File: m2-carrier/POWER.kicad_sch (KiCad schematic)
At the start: 0 parts

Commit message: new stuff
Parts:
- added C16: 4700pF, symbol Device:C_Small
- added C17: 47pF, symbol Device:C_Small
- added C18: 0.1uF, symbol Device:C_Small
- added C19, C20, C21: 47uF, symbol Device:C_Small
- added C21 (x5), C23: 2.2uF, Capacitor_SMD:C_0402_1005Metric, symbol Device:C_Small
- added C24, C27: 47uF, Capacitor_SMD:C_0402_1005Metric, symbol Device:C_Small
- added C28, C29, C32: 100nF, Capacitor_SMD:C_0402_1005Metric, symbol Device:C_Small
- added C3, C5: 10uF, Capacitor_SMD:C_0402_1005Metric_Pad0.74x0.62mm_HandSolder, symbol Device:C_Small
- added C30: 10uF, Capacitor_SMD:C_0402_1005Metric, symbol Device:C_Small
- added C31: C_SS, Capacitor_SMD:C_0402_1005Metric, symbol Device:C_Small
- added D3: D_Small, symbol Device:D_Small
- added D7: B340AG, Diode_SMD:D_SMB, symbol Device:D_Schottky_Small
- added D8: MMBZ5242B, Diode_SMD:D_SOT-23_ANK, symbol Diode:BZV55C12
- added JP1: SolderJumper_3_Open, Jumper:SolderJumper-3_P1.3mm_Open_RoundedPad1.0x1.5mm_NumberLabels, symbol Jumper:SolderJumper_3_Open
- added JP3: IO_EN, Jumper:SolderJumper-2_P1.3mm_Open_RoundedPad1.0x1.5mm, symbol Jumper:SolderJumper_2_Open
- added L2: 8.2uH, Inductor_SMD:L_Bourns_SRP7028A_7.3x6.6mm, symbol Device:L_Small
- added L2: L_Small, symbol Device:L_Small
- added P1: ESC1_VCC, TestPoint:TestPoint_Pad_2.0x2.0mm, symbol hermes_v1-rescue:PAD_SMD-pkl_misc
- added P2: ESC1_GND, TestPoint:TestPoint_Pad_D2.0mm, symbol hermes_v1-rescue:PAD_SMD-pkl_misc
- added P3: LIPO_VCC, TestPoint:TestPoint_Pad_2.0x2.0mm, symbol hermes_v1-rescue:PAD_SMD-pkl_misc
- added P4: LIPO_GND, TestPoint:TestPoint_Pad_D2.0mm, symbol hermes_v1-rescue:PAD_SMD-pkl_misc
- added P5: ESC2_VCC, TestPoint:TestPoint_Pad_2.0x2.0mm, symbol hermes_v1-rescue:PAD_SMD-pkl_misc
- added P6: ESC2_GND, TestPoint:TestPoint_Pad_D2.0mm, symbol hermes_v1-rescue:PAD_SMD-pkl_misc
- added Q1: DMP3013SFV, Package_SON:Diodes_PowerDI3333-8, symbol Transistor_FET:DMP3013SFV
- added R10: 53.6K, symbol Device:R_Small
- added R10: 49.9K, Resistor_SMD:R_0402_1005Metric, symbol Device:R_Small
- added R11: 17.8K, Resistor_SMD:R_0402_1005Metric, symbol Device:R_Small
- added R11: 10.2K, symbol Device:R_Small
- added R17: 12K, Resistor_SMD:R_0402_1005Metric, symbol Device:R_Small
- added R6: 442K, symbol Device:R_Small
- added R7: 90.9K, symbol Device:R_Small
- added R8: 100K, Resistor_SMD:R_0402_1005Metric, symbol Device:R_Small
- added R8: 243K, symbol Device:R_Small
- added R9: 16.9K, symbol Device:R_Small
- added U2: LD1117S33TR_SOT223, Package_TO_SOT_SMD:SOT-223-3_TabPin2, symbol Regulator_Linear:LD1117S33TR_SOT223
- added U3: TPS54560DDAR, Package_SO:Texas_R-PDSO-G8_EP2.95x4.9mm_Mask2.4x3.1mm, symbol Regulator_Switching:TPS54560BDDA
- added U6: LMR16030SDDAR, Package_SO:Texas_HSOP-8-1EP_3.9x4.9mm_P1.27mm_ThermalVias, symbol Regulator_Switching:LMR33630ADDA
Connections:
- new net: C31.1, U6.6 (VCC)
- new net: C29.2, D8.2 (A), Q1.4 (G), R17.1
- new net: C16.1, R9.2
- new net: C21.1, C21.1, C21.1, C21.1, R6.1, U3.2 (VIN)
- new net: R6.2, R7.1, U3.3 (EN)
- new net: C32.2, D7.1 (K), L2.1, U6.8 (SW)
- new net: C32.1, U6.1 (PGND)
- new net: R10.1, U6.4 (PG)
- new net: C18.2, U3.1 (BOOT)
- new net: R8.1, U3.4 (RT/CLK)
- new net: C18.1, D3.1 (K), L2.1, U3.8 (SW)
- new net +12v: C21.1, C23.1, U6.2 (VIN)
- new net +3V3: C5.1, JP3.1 (A), U2.2 (VO)
- new net +5V: JP1.3 (B)
- new net 15V: C29.1, C30.1, D8.1 (K), Q1.1 (S), Q1.2 (S), Q1.3 (S)
- new net 3V3_IO: JP3.2 (B)
- new net 5V_FC_VDD: C24.2, C27.2, L2.2, R8.1
- new net 5V_SERVO_VDD: C19.1, C20.1, C21.1, L2.2, R10.1
- new net COMP: C17.1, R9.1, U3.6 (COMP)
- new net FB: R10.2, R11.1, R11.1, R8.2, U3.5 (FB), U6.5 (FB)
- new net FC_USB_VBUS: JP1.1 (A)
- new net GND: C16.2, C17.2, C19.2, C20.2, C21.2, C21.2, C21.2, C21.2, C21.2, C21.2, C23.2, C24.1, C27.1, C28.2, C3.2, C30.2, C31.2, C5.2, D3.2 (A), D7.2 (A), P2.1 (PAD), P4.1 (PAD), P6.1 (PAD), R10.2, R11.2, R11.2, R17.2, R7.2, R8.2, U2.1 (GND), U3.7 (GND), U3.9 (GND), U6.7 (BOOT), U6.9 (AGND)
- new net REG_5VIN: C3.1, JP1.2 (C), U2.3 (VI)
- new net VCC: C28.1, P1.1 (PAD), P3.1 (PAD), P5.1 (PAD), Q1.5 (D)
- no-connect marks 0 -> 1
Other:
- note added: "+5V @ 3A DC-DC Converter Flight Controller 5V (4.3v-60v Input)"
- note added: "+5V @ 5A DC-DC Converter Servos 5V (7v-60v Input)"
- note added: "2.1mm Tip +12v input Voltage"
- note added: "3A RMS Current 6A I_Saturation"
- note added: "By default, the usb port are connected to the 3.3V LDO If bridged, LDO receives power from buck regulator"
- note added: "C_BOOT"
- note added: "C_SS"
- note added: "Diode to prevent reverse polarity at input"
- note added: "ESC Solder Pads"
- note added: "LiPo Battery Solder Pads"
- note added: "Linear Dropout Regulator - LD1117 - 3.3V 1A"
- note added: "Maximum input voltage: 26V"
- note added: "R_FBB"
- note added: "R_FBT"
- note added: "Rated for 16V"
- note added: "SOT23-3 225mW-300mW"
- note added: "Solder-Jumper for USB_VBUS and 5V"

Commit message: added video IC
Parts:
- added C22, C26: 10uF, Capacitor_SMD:C_0603_1608Metric, symbol Device:C_Small
- added C23, C24: 10uF, Capacitor_SMD:C_0805_2012Metric, symbol Device:C_Small
- added C25: 100nF, symbol Device:C_Small
- added C27, C28, C29: 22uF, Capacitor_SMD:C_0805_2012Metric, symbol Device:C_Small
- added JP1: USB1, Jumper:SolderJumper-3_P1.3mm_Open_RoundedPad1.0x1.5mm_NumberLabels, symbol Jumper:SolderJumper_3_Open
- added L3: 1.5uH, symbol Device:L_Small
- added R13: 10K, symbol Device:R_Small
- added R14: 402K, symbol Device:R_Small
- added R15: 39K, symbol Device:R_Small
- added R16: 100K, symbol Device:R_Small
- added U6: TPS63070RNMR, TPS63070RNMR:RNM0015A, symbol 2023-11-30_05-20-42:TPS63070RNMR
- D3: value D_Small -> B560C
- JP1: value SolderJumper_3_Open -> USB0
- L2: value L_Small -> 7.2uH
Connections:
- net +12v is gone; now on net 15V: C21.1, C23.1, U6.2 (VIN)
- net +5V is gone; now on net 5V_FC_VDD: JP1.3 (B)
- net 3V3_IO is gone; now on net 3V3_FC_VDD: JP3.2 (B)
- net 15V: now also C21.1, C21.1, C21.1, C21.1, R6.1, U3.2 (VIN), C22.1, C23.1, C24.1, R13.1, U6.12 (VIN), U6.13 (VIN)
- net 5V_FC_VDD: now also JP1.3 (B)
- net GND: now also C22.2, C23.2, C24.2, C25.2, C27.2, C28.2, C29.2, R15.2, U6.10 (PGND), U6.15 (VSEL), U6.4 (GND), U6.6 (FB2)
- net +3V3 renamed 3V3_FC_VDD
- net 3V3_FC_VDD: no longer JP3.1 (A)
- net FC_USB_VBUS renamed PWR_USB0_VBUS
- net REG_5VIN renamed 5V_VREG_IN
- net 5V_VREG_IN: now also JP1.2 (C)
- new net: R14.2, R15.1, U6.5 (FB)
- new net: R13.2, U6.1 (PS_SYNC), U6.14 (EN)
- new net: L3.1, U6.11 (L1)
- new net: R16.2, U6.2 (PG)
- new net: L3.2, U6.9 (L2)
- new net 3V3_IO_VDD: JP3.1 (A)
- new net 9V_CAMERA_VDD: C26.1, C27.1, C28.1, C29.1, R14.1, R16.1, U6.7 (VOUT), U6.8 (VOUT)
- new net PWR_USB1_VBUS: JP1.1 (A)
- new net VAUX: C25.1, U6.3 (VAUX)
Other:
- note added: "+9V @ 3.6A DC-DC Converter Camera & VTX 9V (7v-60v Input)"
- note added: "Solder-Jumper for 3V3 IO"
- moved on the sheet: C16, C17, C18, C19, C20, C21, C23, C24, C27, C31, C32, D3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

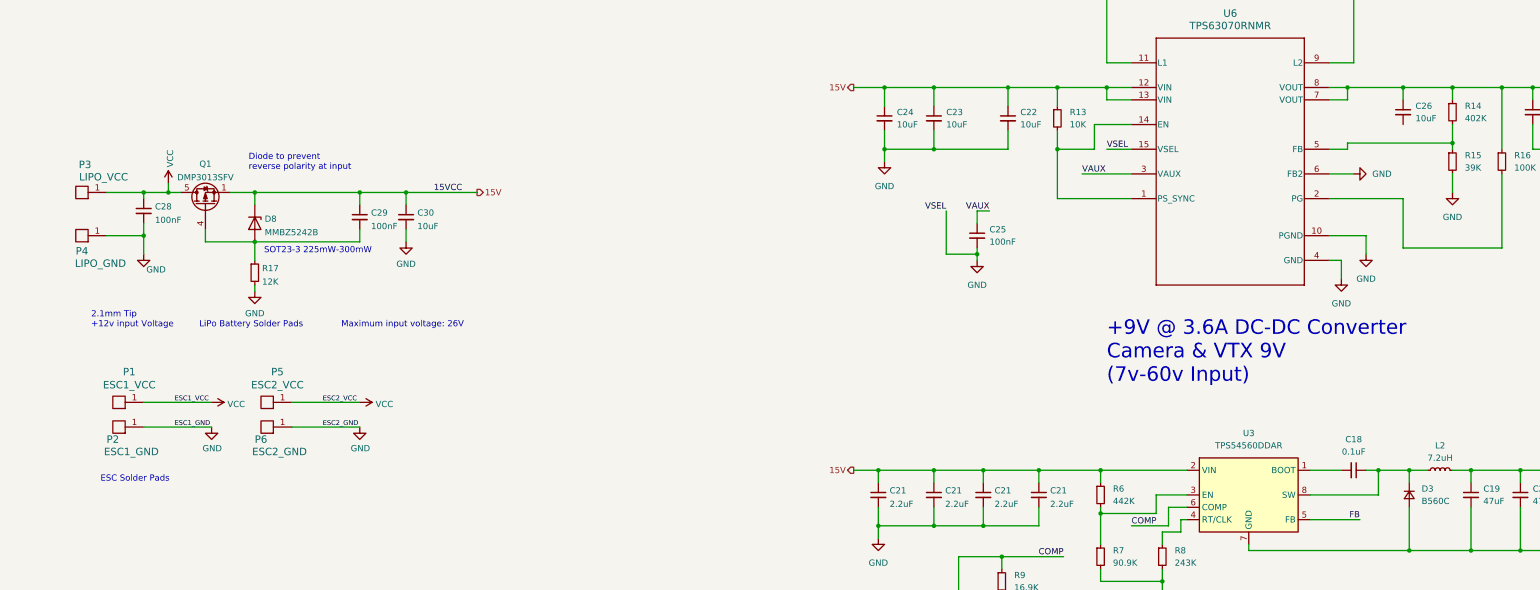
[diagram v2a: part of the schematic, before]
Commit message: Added base board
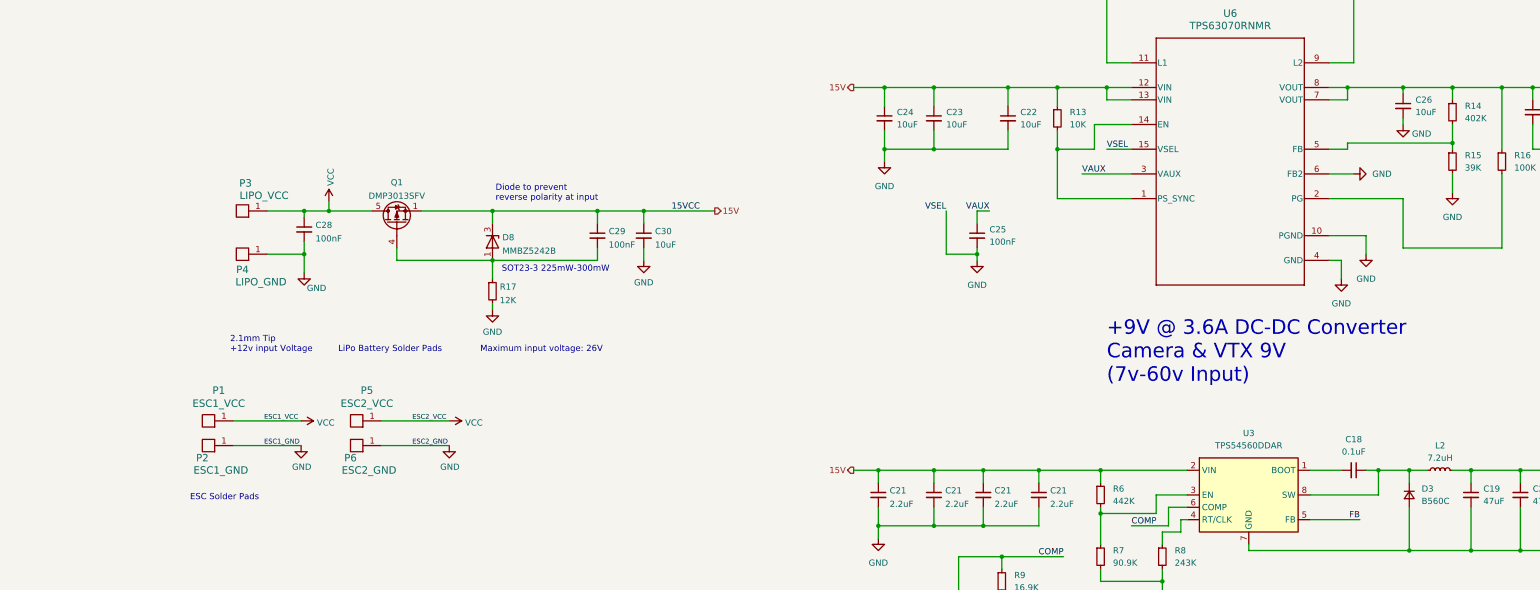
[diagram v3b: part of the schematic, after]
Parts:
- C16, C17, C18, C25: footprint (none) -> Capacitor_SMD:C_0402_1005Metric
- C19, C20, C21: footprint (none) -> Capacitor_SMD:C_0603_1608Metric
- D3: footprint (none) -> Diode_SMD:D_SMC
- D8: footprint Diode_SMD:D_SOT-23_ANK -> Package_TO_SOT_SMD:SOT-23-3
- L2: footprint Inductor_SMD:L_Bourns_SRP7028A_7.3x6.6mm -> Inductor_SMD:L_Coilcraft_XAL4020-XXX
- L2, L3: footprint (none) -> Inductor_SMD:L_Coilcraft_XAL4020-XXX
- R10, R11, R13, R15, R7, R9: footprint (none) -> Resistor_SMD:R_0402_1005Metric
- R14, R16, R6, R8: footprint (none) -> Resistor_SMD:R_0603_1608Metric
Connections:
- net 15V: now also D8.3 (K); no longer D8.1 (K)
- net GND: now also C26.2
- net at C29.2, Q1.4 (G), R17.1: now also D8.1 (A); no longer D8.2 (A)
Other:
- moved on the sheet: C26, C28, C29, C30, P1, P2, P3, P4, P5, P6, Q1, R17

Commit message: added stuff
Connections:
- net FB: no longer R10.2, R11.1, U3.5 (FB)
- new net 5V_FB: R10.2, R11.1, U3.5 (FB)
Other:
- moved on the sheet: D8
